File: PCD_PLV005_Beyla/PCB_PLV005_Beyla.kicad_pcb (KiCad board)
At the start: 2 copper layers, 42 parts, among them J1 PWR/QB, J2 Switch_In, Q1 DMG2302UK-7, Q2 DMP2123L-7, U2 74HC266, U3 74HC08, U4 74HC21, U5 74LVC1G17, U6 LTC6993xS6-1

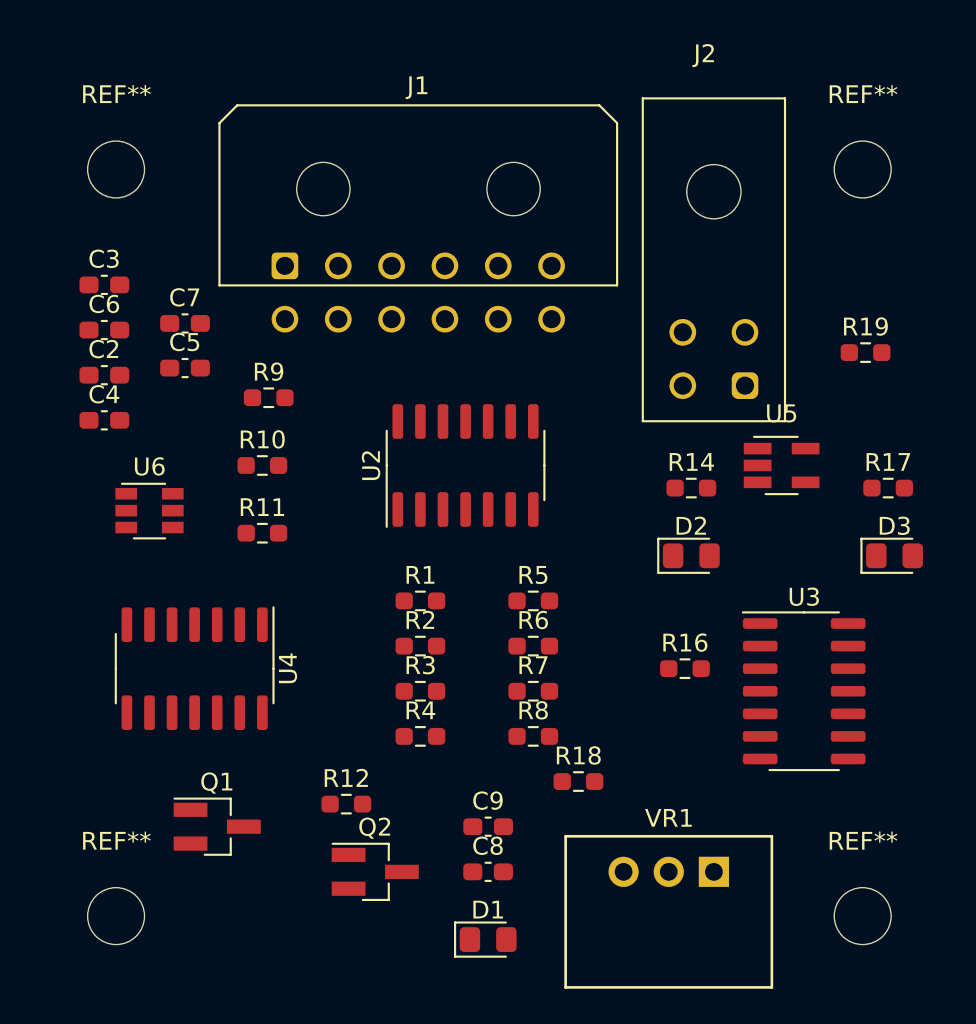
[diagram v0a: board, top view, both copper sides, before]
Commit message: Beyla Layout Fixes, Initial Routing
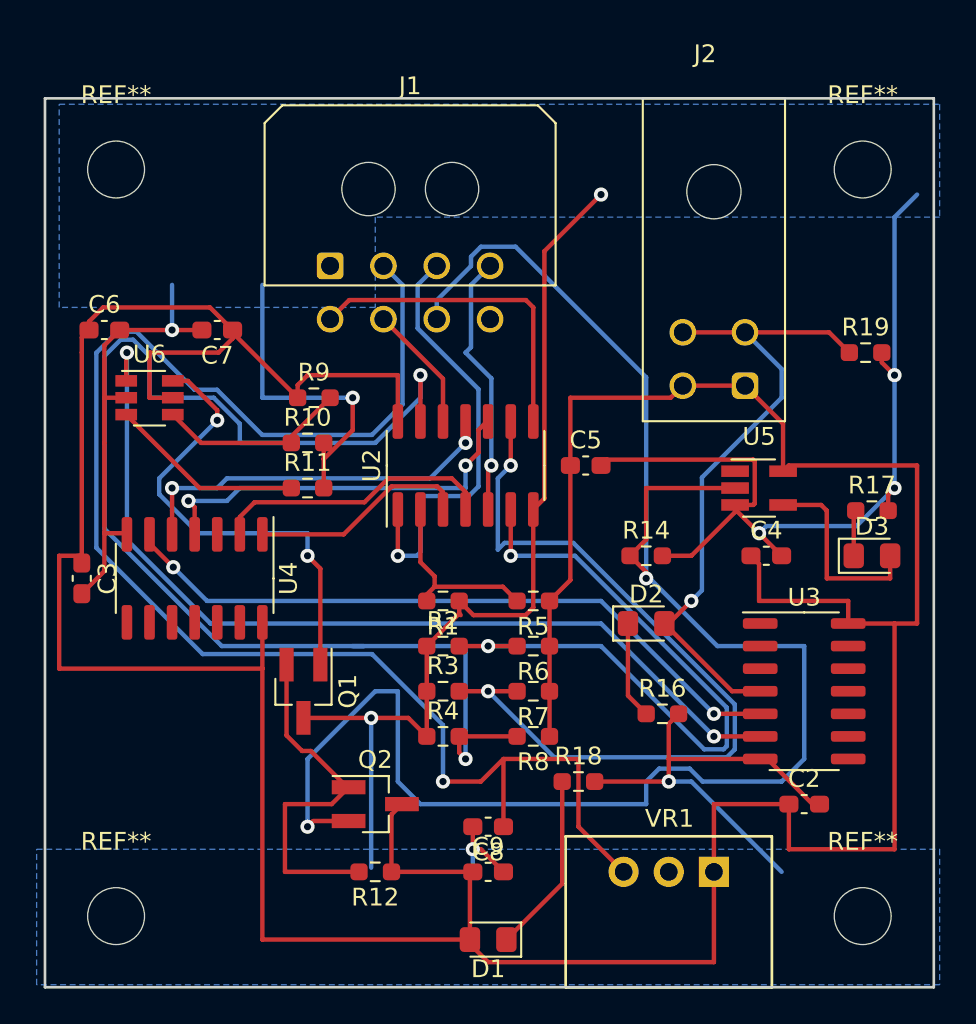
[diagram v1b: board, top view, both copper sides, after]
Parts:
- J1: footprint Connector_Molex:Molex_Micro-Fit_3.0_43045-1200_2x06_P3.00mm_Horizontal -> Connector_Molex:Molex_Micro-Fit_3.0_43045-0800_2x04_P3.00mm_Horizontal
- moved C2 46.2 mm to (92.7, 139.7)
- moved C4 38.0 mm to (90.6, 125.7)
- moved C5 23.2 mm to (80.4, 120.7)
- moved C3 16.6 mm to (52.1, 127.0), turned to 270 degrees
- moved Q1 9.03 mm to (64.5, 133.3), turned to 270 degrees
- moved U6 6.35 mm to (55.9, 116.8)
- moved U4 5.08 mm to (58.4, 127.0)
- moved R14 4.58 mm to (83.8, 125.7)
- moved D2 4.58 mm to (83.8, 129.5)
- moved R12 4.14 mm to (68.6, 143.5), turned to 180 degrees
- moved Q2 3.81 mm to (68.6, 139.7)
- moved R11 3.59 mm to (64.8, 121.9)
- moved R10 2.84 mm to (64.8, 119.4)
- moved R16 2.84 mm to (84.7, 134.6)
- moved J1 2.54 mm to (66.0, 109.4)
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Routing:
- net +5V: track 0.00 -> 221.4 mm
- net GND: track 0.00 -> 178.4 mm, vias 0 -> 9
- net /AvionicsHeartbeatTemplate/HEARTBEAT: track 0.00 -> 100.2 mm, vias 0 -> 2
- net Net-(C8-Pad1): track 0.00 -> 86.2 mm, vias 0 -> 1
- net Net-(R4-Pad2): track 0.00 -> 72.4 mm, vias 0 -> 2
- net Net-(U3-Pad6): track 0.00 -> 52.3 mm, vias 0 -> 2
- net Net-(R3-Pad2): track 0.00 -> 46.1 mm, vias 0 -> 2
- net Net-(R2-Pad2): track 0.00 -> 39.6 mm, vias 0 -> 2
- net Net-(U3-Pad5): track 0.00 -> 38.8 mm, vias 0 -> 2
- net /AvionicsHeartbeatTemplate/HEARTBEAT_INPUT_1: track 0.00 -> 36.9 mm, vias 0 -> 1
- net Net-(Q1-Pad1): track 0.00 -> 26.2 mm, vias 0 -> 2
- net /AvionicsHeartbeatTemplate/HEARTBEAT_ADDRESS_1: track 0.00 -> 24.9 mm, vias 0 -> 1
- net Net-(U2-Pad10): track 0.00 -> 22.2 mm, vias 0 -> 2
- net Net-(U2-Pad11): track 0.00 -> 21.4 mm, vias 0 -> 2
- net Net-(Q1-Pad2): track 0.00 -> 20.6 mm
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- added copper zone on B.Cu, net GND
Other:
- board outline added: 50 x 50 mm

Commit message: Beyla Routing v2
Co-Authored-By: cronin11 <74317819+cronin11@users.noreply.github.com>
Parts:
- added G***: , BoringFootprints:Paradigm_NameBelow_12.7mm, F.Cu at (62.2, 144.8)
- moved C5 8.22 mm to (73.7, 125.3), turned to 180 degrees
- moved Q2 4.02 mm to (69.8, 143.5)
- moved R12 4.02 mm to (69.8, 147.3)
- moved C3 2.54 mm to (52.1, 129.5)
- moved Q1 2.54 mm to (64.5, 135.9)
- moved U4 2.54 mm to (58.4, 129.5)
- moved U2 1.27 mm to (73.7, 119.4), turned to 180 degrees
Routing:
- net +5V: track 221.4 -> 155.6 mm, vias 0 -> 8
- net Net-(R4-Pad2): track 72.4 -> 21.2 mm
- net GND: track 178.4 -> 127.4 mm, vias 9 -> 8
- net /AvionicsHeartbeatTemplate/HEARTBEAT: track 100.2 -> 65.6 mm, vias 2 -> 0
- net Net-(R2-Pad2): track 39.6 -> 19.0 mm
- net Net-(R3-Pad2): track 46.1 -> 26.8 mm
- net /AvionicsHeartbeatTemplate/HEARTBEAT_ADDRESS_3: track 18.5 -> 7.42 mm
- net Net-(D1-Pad1): track 10.2 -> 17.0 mm
- net Net-(C8-Pad1): track 86.2 -> 91.5 mm, vias 1 -> 0
- net Net-(U2-Pad10): track 22.2 -> 17.1 mm, vias 2 -> 0
- net Net-(U2-Pad3): track 12.4 -> 17.1 mm
- net Net-(Q1-Pad2): track 20.6 -> 16.2 mm
- net /AvionicsHeartbeatTemplate/HEARTBEAT_ADDRESS_1: track 24.9 -> 20.7 mm, vias 1 -> 0
- net /AvionicsHeartbeatTemplate/HEARTBEAT_ADDRESS_2: track 15.0 -> 10.8 mm, vias 1 -> 0
- net /AvionicsHeartbeatTemplate/HEARTBEAT_ADDRESS_4: track 7.14 -> 11.1 mm
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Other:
- board text added: "QuantamBeat Interlock "Beyla""
